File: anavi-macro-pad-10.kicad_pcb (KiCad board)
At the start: 2 copper layers, 35 x 49 mm, 8 parts, among them U1 SeeeduinoXIAO

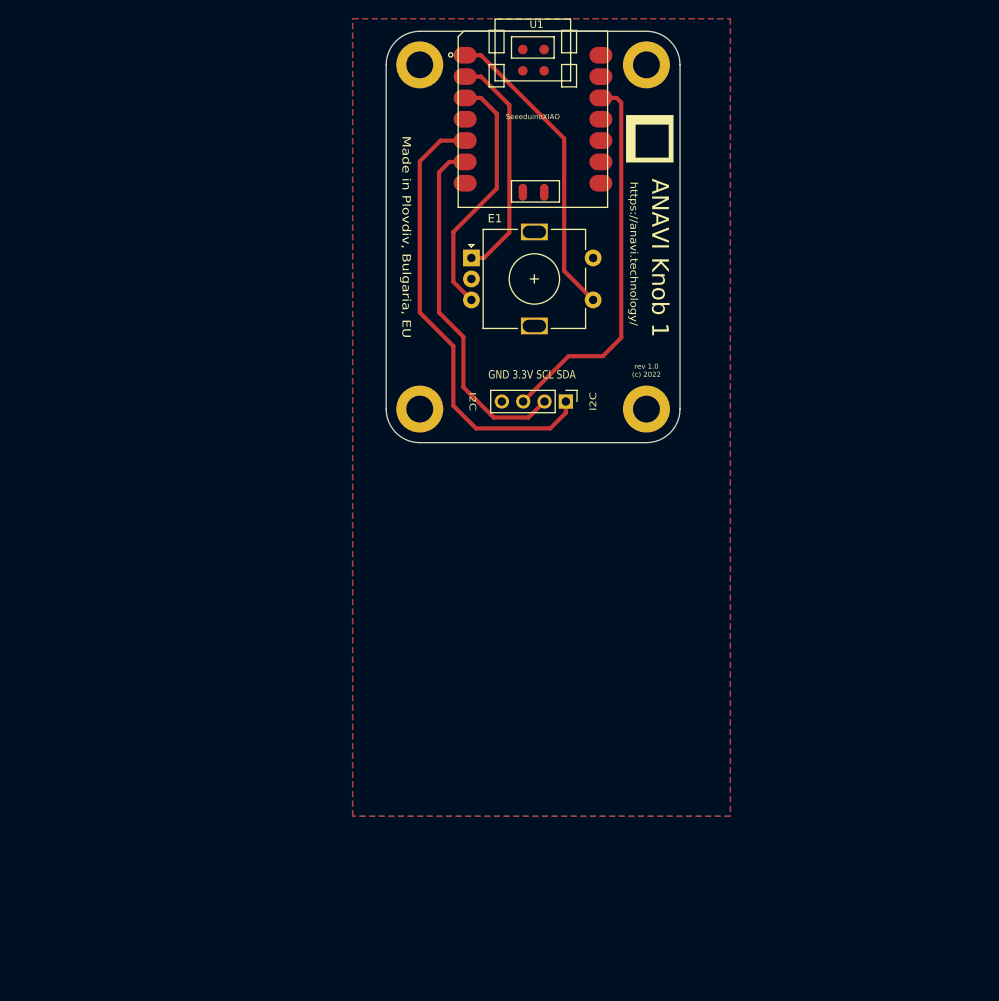
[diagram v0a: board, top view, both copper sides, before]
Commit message: anavi-macro-pad-10: Create PCB
Create printed circuit board.

Signed-off-by: Leon Anavi <leon@anavi.org>
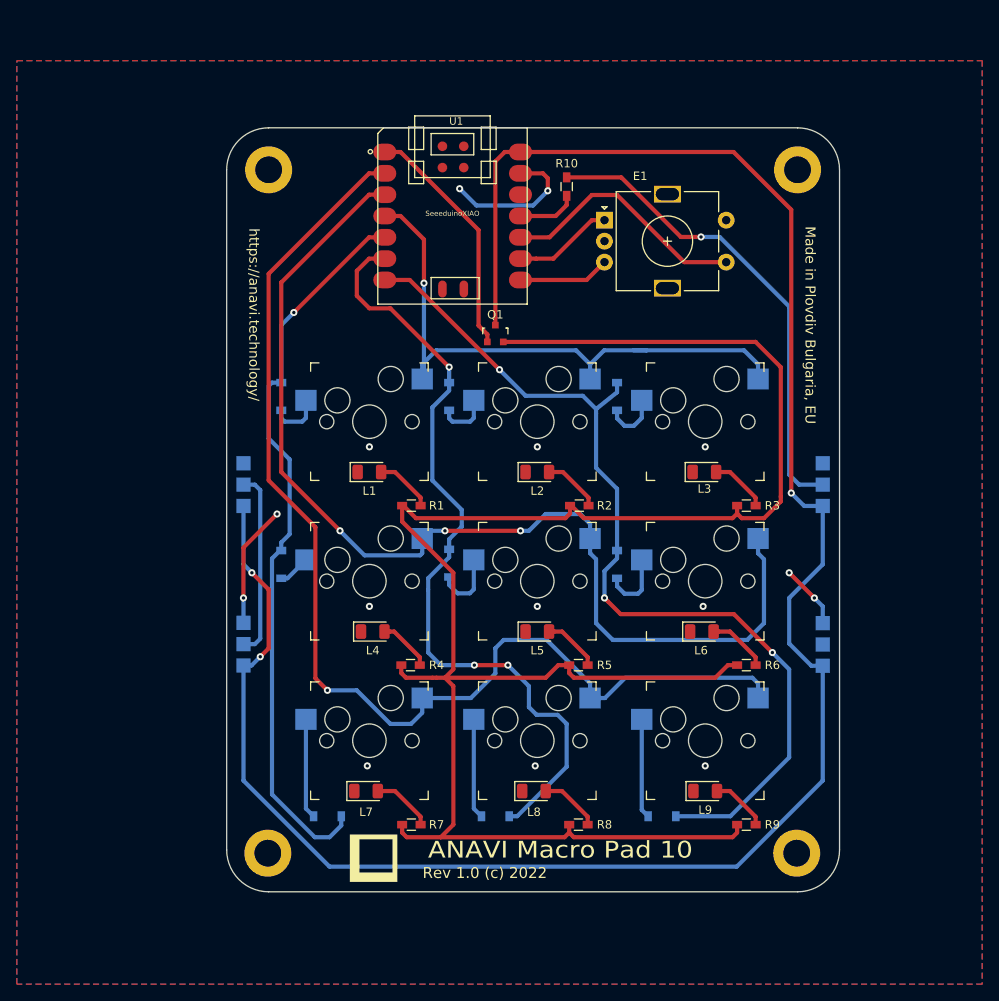
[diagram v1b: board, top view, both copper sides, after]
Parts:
- removed I2C: Conn_01x04_Female, Connector_PinHeader_2.54mm:PinHeader_1x04_P2.54mm_Vertical
- removed the REF** at (113.0, 91.5)
- removed the REF** at (140.0, 91.5)
- removed the REF** at (113.0, 50.5)
- removed the REF** at (140.0, 50.5)
- added D1: 1N4148, Diode_SMD:D_SOD-123, B.Cu at (96.5, 90.0)
- added D2: DIODE, Diode_SMD:D_SOD-123, B.Cu at (116.5, 90.0)
- added D3: DIODE, Diode_SMD:D_SOD-123, B.Cu at (136.5, 90.0)
- added D4: DIODE, Diode_SMD:D_SOD-123, B.Cu at (96.5, 110.0)
- added D5: DIODE, Diode_SMD:D_SOD-123, B.Cu at (116.5, 109.8)
- added D6: DIODE, Diode_SMD:D_SOD-123, B.Cu at (136.5, 110.0)
- added D7: DIODE, Diode_SMD:D_SOD-123, B.Cu at (102.0, 140.0)
- added D8: DIODE, Diode_SMD:D_SOD-123, B.Cu at (122.0, 140.0)
- added D9: DIODE, Diode_SMD:D_SOD-123, B.Cu at (141.8, 140.0)
- added J1: Conn_01x03_Male, led:LedConnector_1x03_P2.54mm, B.Cu at (161.0, 103.0)
- added J2: Conn_01x03_Male, led:LedConnector_1x03_P2.54mm, B.Cu at (92.0, 103.0)
- added J3: Conn_01x03_Male, led:LedConnector_1x03_P2.54mm, B.Cu at (92.0, 122.0)
- added J4: Conn_01x03_Male, led:LedConnector_1x03_P2.54mm, B.Cu at (161.0, 122.1)
- added L1: LED, LED_SMD:LED_1206_3216Metric, F.Cu at (107.0, 99.0)
- added L2: LED, LED_SMD:LED_1206_3216Metric, F.Cu at (127.0, 99.0)
- added L3: LED, LED_SMD:LED_1206_3216Metric, F.Cu at (146.9, 99.0)
- added L4: LED, LED_SMD:LED_1206_3216Metric, F.Cu at (107.4, 118.0)
- added L5: LED, LED_SMD:LED_1206_3216Metric, F.Cu at (127.0, 118.0)
- added L6: LED, LED_SMD:LED_1206_3216Metric, F.Cu at (146.6, 118.0)
- added L7: LED, LED_SMD:LED_1206_3216Metric, F.Cu at (106.6, 137.0)
- added L8: LED, LED_SMD:LED_1206_3216Metric, F.Cu at (126.6, 137.0)
- added L9: LED, LED_SMD:LED_1206_3216Metric, F.Cu at (147.0, 137.0)
- added Q1: Q_NPN_BEC, TO_SOT_Packages_SMD:SOT-23, F.Cu at (122.0, 82.5)
- added R1: 68R, Resistors_SMD:R_0603_HandSoldering, F.Cu at (112.0, 103.0)
- added R10: 470R, Resistors_SMD:R_0603_HandSoldering, F.Cu at (130.5, 65.0)
- added R2: 68R, Resistors_SMD:R_0603_HandSoldering, F.Cu at (132.0, 103.0)
- added R3: 68R, Resistors_SMD:R_0603_HandSoldering, F.Cu at (151.9, 103.0)
- added R4: 68R, Resistors_SMD:R_0603_HandSoldering, F.Cu at (111.9, 122.0)
- added R5: 68R, Resistors_SMD:R_0603_HandSoldering, F.Cu at (131.9, 122.0)
- added R6: 68R, Resistors_SMD:R_0603_HandSoldering, F.Cu at (151.9, 122.0)
- added R7: 68R, Resistors_SMD:R_0603_HandSoldering, F.Cu at (112.0, 141.0)
- added R8: 68R, Resistors_SMD:R_0603_HandSoldering, F.Cu at (131.9, 141.0)
- added R9: 68R, Resistors_SMD:R_0603_HandSoldering, F.Cu at (151.9, 141.0)
- added REF**: MountingHole_3.2mm_M3_DIN965_Pad, MountingHole:MountingHole_3.2mm_M3_DIN965_Pad, F.Cu at (157.9, 144.4)
- added REF**: MountingHole_3.2mm_M3_DIN965_Pad, MountingHole:MountingHole_3.2mm_M3_DIN965_Pad, F.Cu at (94.9, 144.4)
- added REF**: MountingHole_3.2mm_M3_DIN965_Pad, MountingHole:MountingHole_3.2mm_M3_DIN965_Pad, F.Cu at (158.0, 63.0)
- added REF**: MountingHole_3.2mm_M3_DIN965_Pad, MountingHole:MountingHole_3.2mm_M3_DIN965_Pad, F.Cu at (95.0, 63.0)
- added SW1: SW_DIP_x01, keyswitches:Kailh_socket_MX, F.Cu at (107.0, 93.0)
- added SW2: SW_DIP_x01, keyswitches:Kailh_socket_MX, F.Cu at (127.0, 93.0)
- added SW3: SW_DIP_x01, keyswitches:Kailh_socket_MX, F.Cu at (147.0, 93.0)
- added SW4: SW_DIP_x01, keyswitches:Kailh_socket_MX, F.Cu at (107.0, 112.0)
- added SW5: SW_DIP_x01, keyswitches:Kailh_socket_MX, F.Cu at (127.0, 112.0)
- added SW6: SW_DIP_x01, keyswitches:Kailh_socket_MX, F.Cu at (147.0, 112.0)
- added SW7: SW_DIP_x01, keyswitches:Kailh_socket_MX, F.Cu at (107.0, 131.0)
- added SW8: SW_DIP_x01, keyswitches:Kailh_socket_MX, F.Cu at (127.0, 131.0)
- added SW9: SW_DIP_x01, keyswitches:Kailh_socket_MX, F.Cu at (147.0, 131.0)
- moved G*** 91.8 mm to (107.5, 145.0), turned to 0 degrees
- moved E1 16.5 mm to (135.0, 69.0)
- moved U1 15.0 mm to (108.0, 79.0)
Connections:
- U1 pad 1: Net-(E1-PadS1) -> Net-(Q1-Pad1)
- U1 pad 10: (no net) -> Net-(E1-PadS1)
- U1 pad 11: (no net) -> Net-(R10-Pad2)
- U1 pad 12: +3V3 -> (no net)
- U1 pad 14: (no net) -> +5V
- U1 pad 2: Net-(E1-PadA) -> Net-(SW7-Pad1)
- U1 pad 3: Net-(E1-PadB) -> Net-(SW4-Pad1)
- U1 pad 4: (no net) -> Net-(SW1-Pad1)
- U1 pad 7: (no net) -> Net-(D3-Pad2)
- U1 pad 8: (no net) -> Net-(E1-PadB)
- U1 pad 9: (no net) -> Net-(E1-PadA)
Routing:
- net +5V: track 0.00 -> 246.3 mm, vias 0 -> 3
- net Net-(Q1-Pad2): track 0.00 -> 230.9 mm
- net Net-(SW7-Pad1): track 0.00 -> 138.1 mm, vias 0 -> 1
- net Net-(SW4-Pad1): track 0.00 -> 127.8 mm, vias 0 -> 3
- net Net-(D3-Pad2): track 0.00 -> 112.5 mm, vias 0 -> 3
- net Net-(SW1-Pad1): track 0.00 -> 73.2 mm, vias 0 -> 1
- net Net-(J1-Pad2): track 0.00 -> 57.4 mm, vias 0 -> 1
- net Net-(D2-Pad2): track 42.4 -> 95.8 mm, vias 0 -> 3
- net +3V3: track 45.5 -> 0.00 mm
- net GND: track 0.00 -> 39.3 mm, vias 0 -> 7
- net Net-(D1-Pad2): track 54.2 -> 87.9 mm, vias 0 -> 1
- net Net-(Q1-Pad1): track 0.00 -> 28.8 mm
- net Net-(J2-Pad2): track 0.00 -> 22.5 mm
- net Net-(E1-PadB): track 29.8 -> 10.9 mm
- net Net-(E1-PadA): track 27.6 -> 11.9 mm
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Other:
- board size 35 x 49 mm -> 73 x 91 mm
- board text added: "<<<"
- board text added: "ANAVI Macro Pad 10"
- board text added: "Made in Plovdiv Bulgaria, EU"
- board text added: "Rev 1.0 (c) 2022"
- board text removed: "ANAVI Knob 1"
- board text removed: "GND 3.3V SCL SDA"
- board text removed: "I2C"
- board text removed: "Made in Plovdiv, Bulgaria, EU"
- board text removed: "rev 1.0 (c) 2022"

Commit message: anavi-macro-pad-10.kicad_pcb: Finalize PCB
Signed-off-by: Leon Anavi <leon@anavi.org>
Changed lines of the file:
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@@
     (descr "Alps rotary encoder, EC12E... with switch, vertical shaft, http://www.alps.com/prod/info/E/HTML/Encoder/Incremental/EC11/EC11E15204A3.html")
     (tags "rotary encoder")
-    (fp_text reference E1 (at 4.25 -5.25) (layer F.SilkS)
+    (fp_text reference E1 (at 7.5 -5.5) (layer F.SilkS)
       (effects (font (size 1 1) (thickness 0.15)))
     )
@@
     (tags SOT-23)
     (attr smd)
-    (fp_text reference Q1 (at 0 -2.25) (layer F.SilkS)
-      (effects (font (size 1 1) (thickness 0.15)))
-    )
+    (fp_text reference Q1 (at 3 0) (layer F.SilkS)
+      (effects (font (size 1 1) (thickness 0.15)))
+    )

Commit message: anavi-macro-pad-10.kicad_pcb: Rev 1.1
Rev 1.1 of ANAVI Macro Pad 10 with hardware fixes for the WS2812B
LED strips.

Signed-off-by: Leon Anavi <leon@anavi.org>
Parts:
- moved J3 5.18 mm to (93.0, 117.0), turned to 180 degrees
- moved J4 5.18 mm to (160.0, 117.0), turned to 180 degrees
- moved J1 1.00 mm to (160.0, 103.0)
- moved J2 1.00 mm to (93.0, 103.0)
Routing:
- net GND: track 39.3 -> 29.5 mm, vias 7 -> 4
- net +5V: track 246.3 -> 237.3 mm, vias 3 -> 1
- net Net-(J2-Pad2): track 22.5 -> 24.7 mm
- net Net-(D1-Pad2): track 87.9 -> 89.5 mm
- net Net-(J1-Pad2): track 57.4 -> 56.4 mm
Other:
- board text added: "Rev 1.1 (c) 2022"
- board text added: "fafs"
- board text removed: "Rev 1.0 (c) 2022"
